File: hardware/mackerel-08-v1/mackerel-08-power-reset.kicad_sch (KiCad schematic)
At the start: 34 parts, among them J9 DC_Jack, SW1 SW_Push, SW2 SW_SPDT, U17 NE555P

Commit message: Fixed most of the problems with rev 1
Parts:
- removed C25: C_Polarized, Capacitor_THT:CP_Radial_D10.0mm_P5.00mm, symbol Device:C_Polarized
- removed J9: DC_Jack, Connector_BarrelJack:BarrelJack_GCT_DCJ200-10-A_Horizontal, symbol mackerel-68k-symbols:DC_Jack
- added J4: Barrel_Jack_MountingPin, Connector_BarrelJack:BarrelJack_Horizontal, symbol Connector:Barrel_Jack_MountingPin
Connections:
- net GND: now also J4.2
- net at SW2.2 (B): now also J4.1
- no-connect marks 3 -> 4

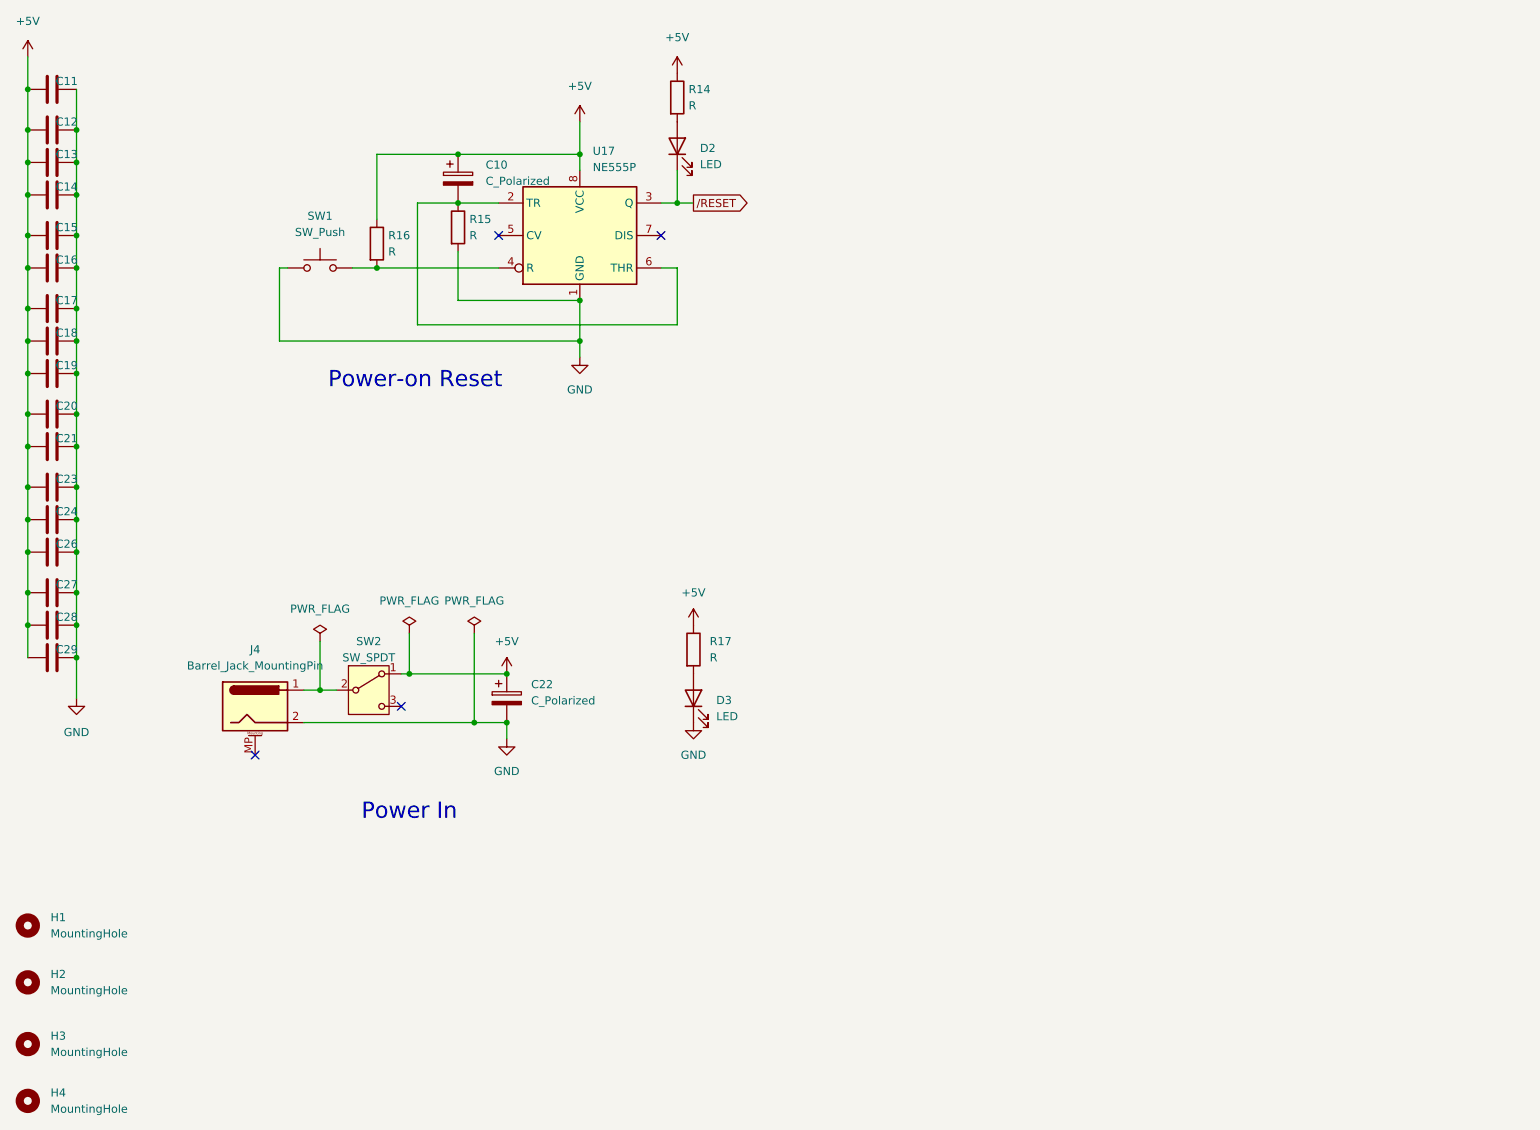
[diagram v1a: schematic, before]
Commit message: Mack-08 1.1 schematic fixes done, needs final routing
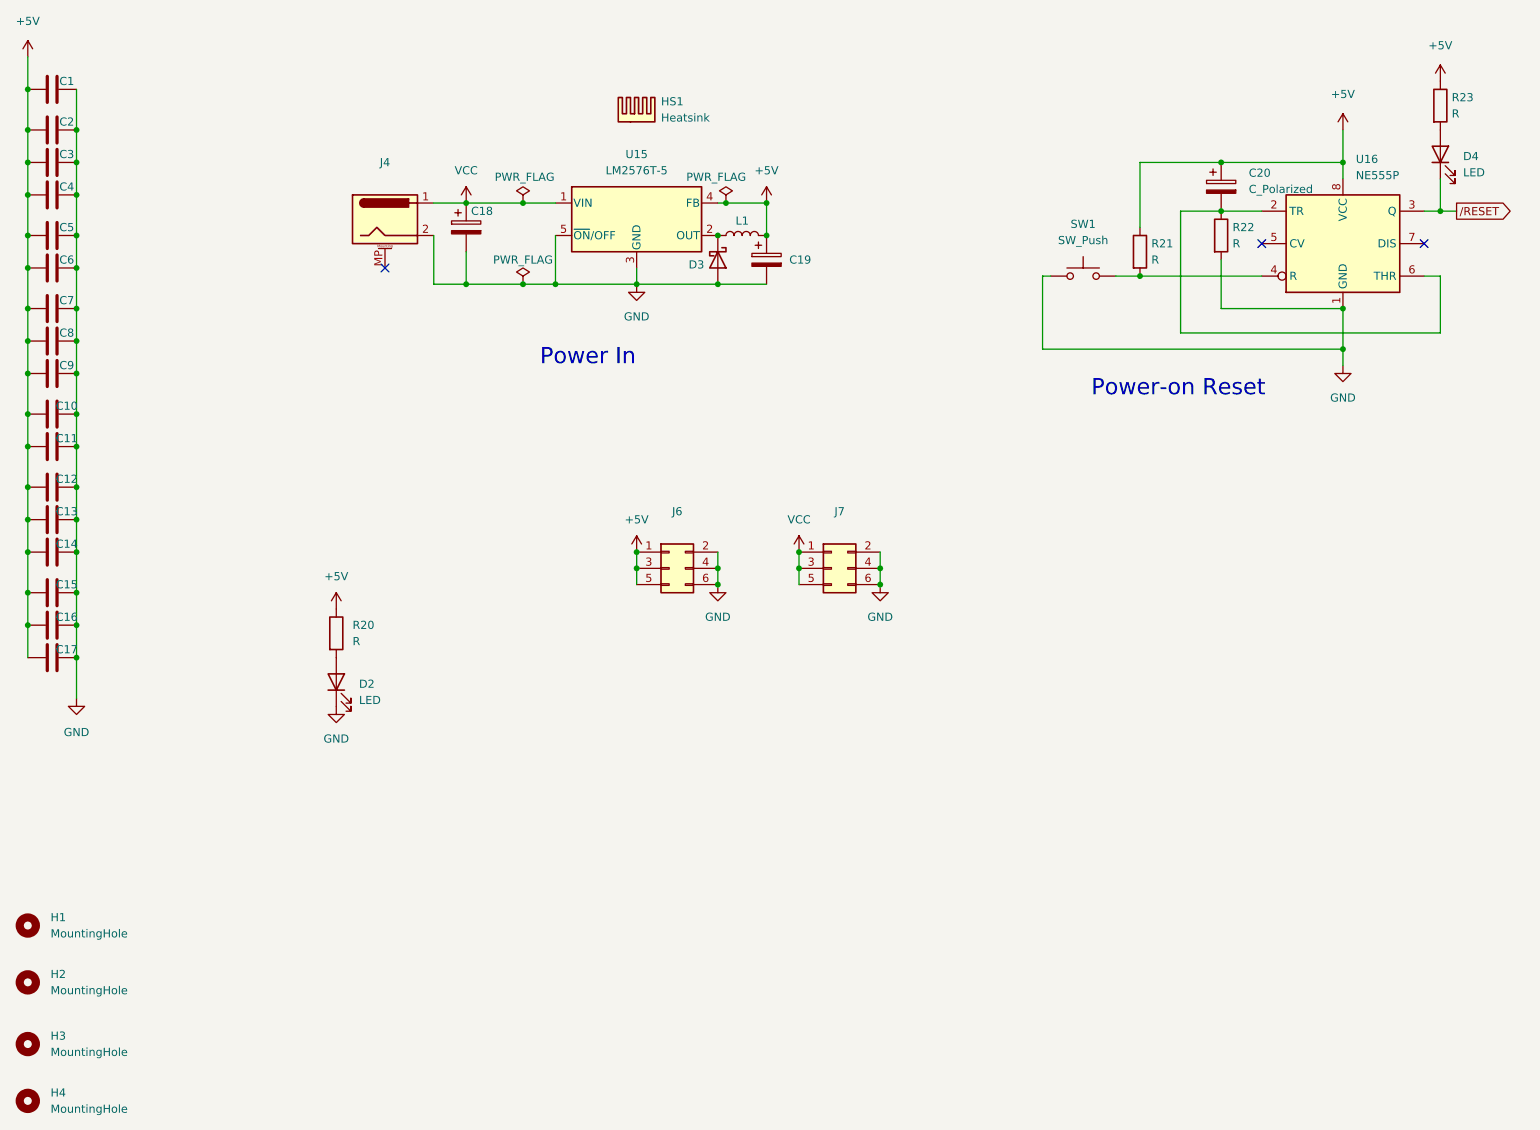
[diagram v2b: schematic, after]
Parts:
- removed C22: C_Polarized, Capacitor_THT:CP_Radial_D10.0mm_P5.00mm, symbol Device:C_Polarized
- removed SW2: SW_SPDT, herring:SW_Mini_Toggle, symbol Switch:SW_SPDT
- added C18, C19: C_Polarized, Capacitor_THT:CP_Radial_D10.0mm_P5.00mm, symbol Device:C_Polarized
- added D3: D_Schottky, Diode_THT:D_DO-27_P15.24mm_Horizontal, symbol Device:D_Schottky
- added HS1: Heatsink, Heatsink:Heatsink_Stonecold_HS-S02_13.21x9.53mm, symbol Mechanical:Heatsink
- added J6, J7: Conn_02x03_Odd_Even, Connector_PinHeader_2.54mm:PinHeader_2x03_P2.54mm_Vertical, symbol Connector_Generic:Conn_02x03_Odd_Even
- added L1: L, Inductor_THT:L_Radial_D10.0mm_P5.00mm_Fastron_07M, symbol Device:L
- added U15: LM2576T-5, Package_TO_SOT_THT:TO-220-5_Vertical, symbol Regulator_Switching:LM2576T-5
- renumbered C11 to C1, C20 to C10, C21 to C11, C23 to C12, C24 to C13, C26 to C14, C27 to C15, C28 to C16, C29 to C17, C12 to C2, C10 to C20, C13 to C3, C14 to C4, C15 to C5, C16 to C6, C17 to C7, C18 to C8, C19 to C9, D3 to D2, D2 to D4, R17 to R20, R16 to R21, R15 to R22, R14 to R23, U17 to U16
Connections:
- net +5V: now also C19.1, J6.1 (Pin_1), J6.3 (Pin_3), J6.5 (Pin_5), L1.2, U15.4 (FB)
- net GND: now also C18.2, C19.2, D3.2 (A), J6.2 (Pin_2), J6.4 (Pin_4), J6.6 (Pin_6), J7.2 (Pin_2), J7.4 (Pin_4), J7.6 (Pin_6), U15.3 (GND), U15.5 (~{ON}/OFF)
- net VCC: now reaches J4.1
- net VCC: now also C18.1, J7.1 (Pin_1), J7.3 (Pin_3), J7.5 (Pin_5), U15.1 (VIN)
- new net: D3.1 (K), L1.1, U15.2 (OUT)
- no-connect marks 4 -> 3
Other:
- moved on the sheet: C20, D2, D4, R20, R21, R22, R23, SW1, U16

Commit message: Mack-08 rev 1.1 routed
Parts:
- C18, C19: value C_Polarized -> 1000uF
- D3: value D_Schottky -> 1N5822
- L1: value L -> 100uH
- R20, R21, R22, R23: footprint Resistor_THT:R_Axial_DIN0207_L6.3mm_D2.5mm_P7.62mm_Horizontal -> Resistor_SMD:R_1206_3216Metric_Pad1.30x1.75mm_HandSolder
- renumbered J4 to J5
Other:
- note added: "Extra Power Pins"
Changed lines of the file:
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@@
 		)
 	)
+	(text "Extra Power Pins"
+		(exclude_from_sim no)
+		(at 138.43 120.904 0)
+		(effects
+			(font
+				(size 2.54 2.54)
+			)
+		)
+	)
 	(global_label "{slash}RESET"
 		(shape output)
@@
 			)
 		)
-		(property "Footprint" "Resistor_THT:R_Axial_DIN0207_L6.3mm_D2.5mm_P7.62mm_Horizontal"
+		(property "Footprint" "Resistor_SMD:R_1206_3216Metric_Pad1.30x1.75mm_HandSolder"
 			(at 207.772 53.34 90)
 			(effects
@@
 			)
 		)
-		(property "Footprint" "Resistor_THT:R_Axial_DIN0207_L6.3mm_D2.5mm_P7.62mm_Horizontal"
+		(property "Footprint" "Resistor_SMD:R_1206_3216Metric_Pad1.30x1.75mm_HandSolder"
 			(at 195.072 55.88 90)
 			(effects
@@
 		(dnp no)
 		(fields_autoplaced yes)
-		(property "Reference" "#PWR072"
+		(property "Reference" "#PWR057"
 			(at 130.81 114.3 0)
 			(effects
@@
 			(project ""
 				(path "/d8b1bce0-db11-4fa6-8e54-fcae9a8fcfc2/7a389a7c-8317-4082-87da-094545447ed4"
-					(reference "#PWR072")
+					(reference "#PWR057")
 					(unit 1)
 				)
@@
 		(dnp no)
 		(property "Reference" "L1"
-			(at 134.62 51.054 90)
+			(at 134.366 54.356 90)
 			(effects
 				(font
@@
 			)
 		)
-		(property "Value" "L"
+		(property "Value" "100uH"
 			(at 134.62 50.8 90)
 			(effects
@@
 					(size 1.27 1.27)
 				)
-				(hide yes)
 			)
 		)
@@
 		(dnp no)
 		(property "Reference" "D3"
-			(at 126.238 57.912 90)
+			(at 126.238 57.658 90)
 			(effects
 				(font
@@
 			)
 		)
-		(property "Value" "D_Schottky"
-			(at 133.35 58.1024 90)
+		(property "Value" "1N5822"
+			(at 122.936 59.944 90)
 			(effects
 				(font
@@
 				)
 				(justify left)
-				(hide yes)
 			)
 		)
@@
 			)
 		)
-		(property "Footprint" "Resistor_THT:R_Axial_DIN0207_L6.3mm_D2.5mm_P7.62mm_Horizontal"
+		(property "Footprint" "Resistor_SMD:R_1206_3216Metric_Pad1.30x1.75mm_HandSolder"
 			(at 69.342 115.57 90)
 			(effects
@@
 		(dnp no)
 		(fields_autoplaced yes)
-		(property "Reference" "#PWR049"
+		(property "Reference" "#PWR051"
 			(at 30.48 132.08 0)
 			(effects
@@
 			(project "mackerel-08-v1"
 				(path "/d8b1bce0-db11-4fa6-8e54-fcae9a8fcfc2/7a389a7c-8317-4082-87da-094545447ed4"
-					(reference "#PWR049")
+					(reference "#PWR051")
 					(unit 1)
 				)
@@
 			)
 		)
-		(property "Footprint" "Resistor_THT:R_Axial_DIN0207_L6.3mm_D2.5mm_P7.62mm_Horizontal"
+		(property "Footprint" "Resistor_SMD:R_1206_3216Metric_Pad1.30x1.75mm_HandSolder"
 			(at 242.062 33.02 90)
 			(effects
@@
 		(dnp no)
 		(fields_autoplaced yes)
-		(property "Reference" "#PWR052"
+		(property "Reference" "#PWR054"
 			(at 91.44 52.07 0)
 			(effects
@@
 			(project "mackerel-08-v1"
 				(path "/d8b1bce0-db11-4fa6-8e54-fcae9a8fcfc2/7a389a7c-8317-4082-87da-094545447ed4"
-					(reference "#PWR052")
+					(reference "#PWR054")
 					(unit 1)
 				)
@@
 		(dnp no)
 		(fields_autoplaced yes)
-		(property "Reference" "#PWR071"
+		(property "Reference" "#PWR056"
 			(at 118.11 106.68 0)
 			(effects
@@
 			(project ""
 				(path "/d8b1bce0-db11-4fa6-8e54-fcae9a8fcfc2/7a389a7c-8317-4082-87da-094545447ed4"
-					(reference "#PWR071")
+					(reference "#PWR056")
 					(unit 1)
 				)
@@
 			)
 		)
-		(property "Value" "C_Polarized"
-			(at 95.25 52.4509 0)
+		(property "Value" "1000uF"
+			(at 93.98 52.324 0)
 			(effects
 				(font
@@
 				)
 				(justify left)
-				(hide yes)
 			)
 		)
@@
 		(dnp no)
 		(fields_autoplaced yes)
-		(property "Reference" "#PWR057"
+		(property "Reference" "#PWR063"
 			(at 243.84 33.02 0)
 			(effects
@@
 			(project "mackerel-08-v1"
 				(path "/d8b1bce0-db11-4fa6-8e54-fcae9a8fcfc2/7a389a7c-8317-4082-87da-094545447ed4"
-					(reference "#PWR057")
+					(reference "#PWR063")
 					(unit 1)
 				)
@@
 		(dnp no)
 		(fields_autoplaced yes)
-		(property "Reference" "#PWR073"
+		(property "Reference" "#PWR059"
 			(at 143.51 106.68 0)
 			(effects
@@
 			(project ""
 				(path "/d8b1bce0-db11-4fa6-8e54-fcae9a8fcfc2/7a389a7c-8317-4082-87da-094545447ed4"
-					(reference "#PWR073")
+					(reference "#PWR059")
 					(unit 1)
 				)
@@
 		(dnp no)
 		(fields_autoplaced yes)
-		(property "Reference" "#PWR054"
+		(property "Reference" "#PWR058"
 			(at 138.43 52.07 0)
 			(effects
@@
 			(project "mackerel-08-v1"
 				(path "/d8b1bce0-db11-4fa6-8e54-fcae9a8fcfc2/7a389a7c-8317-4082-87da-094545447ed4"
-					(reference "#PWR054")
+					(reference "#PWR058")
 					(unit 1)
 				)
@@
 		(dnp no)
 		(fields_autoplaced yes)
-		(property "Reference" "#PWR050"
+		(property "Reference" "#PWR052"
 			(at 71.12 115.57 0)
 			(effects
@@
 			(project "mackerel-08-v1"
 				(path "/d8b1bce0-db11-4fa6-8e54-fcae9a8fcfc2/7a389a7c-8317-4082-87da-094545447ed4"
-					(reference "#PWR050")
+					(reference "#PWR052")
 					(unit 1)
 				)
@@
 		(dnp no)
 		(fields_autoplaced yes)
-		(property "Reference" "J4"
+		(property "Reference" "J5"
 			(at 78.74 41.91 0)
 			(effects
@@
 			(project "mackerel-08-v1"
 				(path "/d8b1bce0-db11-4fa6-8e54-fcae9a8fcfc2/7a389a7c-8317-4082-87da-094545447ed4"
-					(reference "J4")
+					(reference "J5")
 					(unit 1)
 				)
@@
 		(dnp no)
 		(fields_autoplaced yes)
-		(property "Reference" "#PWR056"
+		(property "Reference" "#PWR062"
 			(at 228.6 80.01 0)
 			(effects
@@
 			(project "mackerel-08-v1"
 				(path "/d8b1bce0-db11-4fa6-8e54-fcae9a8fcfc2/7a389a7c-8317-4082-87da-094545447ed4"
-					(reference "#PWR056")
+					(reference "#PWR062")
 					(unit 1)
 				)
@@
 		(dnp no)
 		(fields_autoplaced yes)
-		(property "Reference" "#PWR051"
+		(property "Reference" "#PWR053"
 			(at 71.12 133.35 0)
 			(effects
@@
 			(project "mackerel-08-v1"
 				(path "/d8b1bce0-db11-4fa6-8e54-fcae9a8fcfc2/7a389a7c-8317-4082-87da-094545447ed4"
-					(reference "#PWR051")
+					(reference "#PWR053")
 					(unit 1)
 				)
@@
 		(dnp no)
 		(fields_autoplaced yes)
-		(property "Reference" "#PWR055"
+		(property "Reference" "#PWR061"
 			(at 228.6 40.64 0)
 			(effects
@@
 			(project "mackerel-08-v1"
 				(path "/d8b1bce0-db11-4fa6-8e54-fcae9a8fcfc2/7a389a7c-8317-4082-87da-094545447ed4"
-					(reference "#PWR055")
+					(reference "#PWR061")
 					(unit 1)
 				)
@@
 		(dnp no)
 		(property "Reference" "C19"
-			(at 141.986 57.15 0)
+			(at 139.192 54.61 0)
 			(effects
 				(font
@@
 			)
 		)
-		(property "Value" "C_Polarized"
-			(at 142.24 57.5309 0)
+		(property "Value" "1000uF"
+			(at 141.478 57.404 0)
 			(effects
 				(font
@@
 				)
 				(justify left)
-				(hide yes)
 			)
 		)
@@
 		(dnp no)
 		(fields_autoplaced yes)
-		(property "Reference" "#PWR048"
+		(property "Reference" "#PWR050"
 			(at 22.86 29.21 0)
 			(effects
@@
 			(project "mackerel-08-v1"
 				(path "/d8b1bce0-db11-4fa6-8e54-fcae9a8fcfc2/7a389a7c-8317-4082-87da-094545447ed4"
-					(reference "#PWR048")
+					(reference "#PWR050")
 					(unit 1)
 				)
@@
 		(dnp no)
 		(fields_autoplaced yes)
-		(property "Reference" "#PWR074"
+		(property "Reference" "#PWR060"
 			(at 156.21 114.3 0)
 			(effects
@@
 			(project ""
 				(path "/d8b1bce0-db11-4fa6-8e54-fcae9a8fcfc2/7a389a7c-8317-4082-87da-094545447ed4"
-					(reference "#PWR074")
+					(reference "#PWR060")
 					(unit 1)
 				)
@@
 		(dnp no)
 		(fields_autoplaced yes)
-		(property "Reference" "#PWR053"
+		(property "Reference" "#PWR055"
 			(at 118.11 67.31 0)
 			(effects
@@
 			(project "mackerel-08-v1"
 				(path "/d8b1bce0-db11-4fa6-8e54-fcae9a8fcfc2/7a389a7c-8317-4082-87da-094545447ed4"
-					(reference "#PWR053")
+					(reference "#PWR055")
 					(unit 1)
 				)

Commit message: Mackerel-08 rev 1.1 release
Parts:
- added C21, C22: C_Polarized, Capacitor_THT:CP_Radial_D5.0mm_P2.50mm, symbol Device:C_Polarized
- added J10: Conn_02x03_Odd_Even, Connector_PinHeader_2.54mm:PinHeader_2x03_P2.54mm_Vertical, symbol Connector_Generic:Conn_02x03_Odd_Even
- added U17: ~, Package_TO_SOT_SMD:TO-252-2, symbol AP1084:AP1084
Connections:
- net +5V: now also C21.1, U17.3 (Vin)
- net GND: now also C21.2, C22.2, J10.2 (Pin_2), J10.4 (Pin_4), J10.6 (Pin_6), U17.1 (GND)
- new net +3.3V: C22.1, J10.1 (Pin_1), J10.3 (Pin_3), J10.5 (Pin_5), U17.2 (Vout)
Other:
- note added: "Accessory 3.3v regulator"

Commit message: Add Mackerel-08 BOM list
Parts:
- C1, C10, C11, C12, C13, C14, C15, C16, C17, C2, C3, C4, C5, C6, C7, C8, C9: value C -> 0.1uF
- C20, C21, C22: value C_Polarized -> 10uF
- R20, R23: value R -> 1k
- R21, R22: value R -> 10k
- U17: value ~ -> AP1084
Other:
- note added: "Decoupling caps C1-C17 are all 0.1uF"
- title: Mackerel-08 SBC v1 -> Mackerel-08 SBC v1.1
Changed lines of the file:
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@@
 	(paper "A")
 	(title_block
-		(title "Mackerel-08 SBC v1")
+		(title "Mackerel-08 SBC v1.1")
 		(date "2024-08-22")
 		(rev "1.1")
@@
 		)
 	)
+	(text "Decoupling caps C1-C17 are all 0.1uF"
+		(exclude_from_sim no)
+		(at 56.134 77.978 0)
+		(effects
+			(font
+				(size 1.27 1.27)
+			)
+		)
+	)
 	(text "Power In"
 		(exclude_from_sim no)
@@
 			)
 		)
-		(property "Value" "R"
+		(property "Value" "10k"
 			(at 211.328 54.6099 0)
 			(effects
@@
 			)
 		)
-		(property "Value" "R"
+		(property "Value" "10k"
 			(at 198.628 57.1499 0)
 			(effects
@@
 			)
 		)
-		(property "Value" "C"
+		(property "Value" "0.1uF"
 			(at 26.67 98.552 90)
 			(effects
@@
 			)
 		)
-		(property "Value" "~"
-			(at 222.25 107.95 0)
+		(property "Value" "AP1084"
+			(at 222.25 110.49 0)
 			(effects
 				(font
@@
 		(dnp no)
 		(property "Reference" "C21"
-			(at 209.804 114.554 0)
+			(at 202.438 114.046 0)
 			(effects
 				(font
@@
 			)
 		)
-		(property "Value" "C_Polarized"
-			(at 213.36 117.2209 0)
+		(property "Value" "10uF"
+			(at 201.676 116.84 0)
 			(effects
 				(font
@@
 				)
 				(justify left)
-				(hide yes)
 			)
 		)
@@
 			)
 		)
-		(property "Value" "R"
+		(property "Value" "1k"
 			(at 73.66 116.8399 0)
 			(effects
@@
 			)
 		)
-		(property "Value" "C"
+		(property "Value" "0.1uF"
 			(at 26.67 49.022 90)
 			(effects
@@
 			)
 		)
-		(property "Value" "C"
+		(property "Value" "0.1uF"
 			(at 26.67 37.592 90)
 			(effects
@@
 			)
 		)
-		(property "Value" "C"
+		(property "Value" "0.1uF"
 			(at 26.67 93.472 90)
 			(effects
@@
 			)
 		)
-		(property "Value" "R"
+		(property "Value" "1k"
 			(at 245.618 34.2899 0)
 			(effects
@@
 			)
 		)
-		(property "Value" "C"
+		(property "Value" "0.1uF"
 			(at 26.67 65.532 90)
 			(effects
@@
 			)
 		)
-		(property "Value" "C"
+		(property "Value" "0.1uF"
 			(at 26.67 76.962 90)
 			(effects
@@
 			)
 		)
-		(property "Value" "C_Polarized"
+		(property "Value" "10uF"
 			(at 213.868 46.1009 0)
 			(effects
@@
 			)
 		)
-		(property "Value" "C"
+		(property "Value" "0.1uF"
 			(at 26.67 54.102 90)
 			(effects
@@
 			)
 		)
-		(property "Value" "C"
+		(property "Value" "0.1uF"
 			(at 26.67 32.512 90)
 			(effects
@@
 			)
 		)
-		(property "Value" "C"
+		(property "Value" "0.1uF"
 			(at 26.67 109.982 90)
 			(effects
@@
 			)
 		)
-		(property "Value" "C"
+		(property "Value" "0.1uF"
 			(at 26.67 115.062 90)
 			(effects
@@
 			)
 		)
-		(property "Value" "C"
+		(property "Value" "0.1uF"
 			(at 26.67 42.672 90)
 			(effects
@@
 			)
 		)
-		(property "Value" "C"
+		(property "Value" "0.1uF"
 			(at 26.67 88.392 90)
 			(effects
@@
 		(dnp no)
 		(property "Reference" "C22"
-			(at 235.458 114.554 0)
+			(at 237.998 114.554 0)
 			(effects
 				(font
@@
 			)
 		)
-		(property "Value" "C_Polarized"
-			(at 238.76 117.2209 0)
+		(property "Value" "10uF"
+			(at 237.998 117.348 0)
 			(effects
 				(font
@@
 				)
 				(justify left)
-				(hide yes)
 			)
 		)
@@
 			)
 		)
-		(property "Value" "C"
+		(property "Value" "0.1uF"
 			(at 26.67 70.612 90)
 			(effects
@@
 			)
 		)
-		(property "Value" "C"
+		(property "Value" "0.1uF"
 			(at 26.67 104.902 90)
 			(effects
@@
 			)
 		)
-		(property "Value" "C"
+		(property "Value" "0.1uF"
 			(at 26.67 60.452 90)
 			(effects
@@
 			)
 		)
-		(property "Value" "C"
+		(property "Value" "0.1uF"
 			(at 26.67 82.042 90)
 			(effects
@@
 			)
 		)
-		(property "Value" "C"
+		(property "Value" "0.1uF"
 			(at 26.67 26.162 90)
 			(effects
